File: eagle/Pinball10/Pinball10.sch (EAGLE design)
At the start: 49 parts, among them J1 UB-M5BR-DM14, Q1 MOSFET-NCHANNEL2N7002PW, U1 CYBLE-014008-00, U2 MMA8452Q, U3 PCA9306, U4 V_REG_317SMD

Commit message: labeling done
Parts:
- GND: value PTR1PAD1-13 -> GND
- renumbered JP1 to M0+, JP2 to M1+, LEDBANK0 to BANK0, TP1 to V50, TP2 to GND, TP3 to V33
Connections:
- removed net VDD: LCD.2
- net V50: now also LCD.2
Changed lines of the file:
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@@
 <part name="U$1" library="arh" deviceset="9X2" device=""/>
 <part name="J1" library="con-usb" deviceset="UB-M5BR-DM14" device=""/>
-<part name="LEDBANK0" library="SparkFun-Connectors" deviceset="M08X2" device=""/>
+<part name="BANK0" library="SparkFun-Connectors" deviceset="M08X2" device="" value="M08X2"/>
 <part name="R1" library="SparkFun" deviceset="RESISTOR" device=""/>
 <part name="R2" library="SparkFun" deviceset="RESISTOR" device=""/>
@@
 <part name="R11" library="SparkFun-Resistors" deviceset="RESISTOR" device="0805-RES"/>
 <part name="S1" library="SparkFun-Electromechanical" deviceset="TAC_SWITCH" device="SMD" value="TAC_SWITCHSMD"/>
-<part name="JP1" library="SparkFun-Connectors" deviceset="M02" device="PTH"/>
-<part name="JP2" library="SparkFun-Connectors" deviceset="M02" device="PTH"/>
+<part name="M0+" library="SparkFun-Connectors" deviceset="M02" device="PTH"/>
+<part name="M1+" library="SparkFun-Connectors" deviceset="M02" device="PTH"/>
 <part name="JP3" library="SparkFun-Connectors" deviceset="M05" device="LOCK"/>
 <part name="R12" library="SparkFun-Passives" deviceset="RESISTOR" device="0805-RES"/>
 <part name="R13" library="SparkFun-Passives" deviceset="RESISTOR" device="0805-RES"/>
-<part name="TP1" library="testpad" deviceset="PTR1" device="PAD1-13"/>
-<part name="TP2" library="testpad" deviceset="PTR1" device="PAD1-13"/>
-<part name="TP3" library="testpad" deviceset="PTR1" device="PAD1-13"/>
+<part name="V50" library="testpad" deviceset="PTR1" device="PAD1-13"/>
+<part name="GND" library="testpad" deviceset="PTR1" device="PAD1-13" value="GND"/>
+<part name="V33" library="testpad" deviceset="PTR1" device="PAD1-13"/>
 </parts>
 <sheets>
@@
 </segment>
 </net>
-<net name="VDD" class="0">
-<segment>
-<pinref part="LCD" gate="G$1" pin="2"/>
-<wire x1="86.36" y1="0" x2="101.6" y2="0" width="0.1524" layer="91"/>
-<label x="88.9" y="0" size="1.778" layer="95"/>
-</segment>
-</net>
 <net name="LEDCOL2" class="0">
 <segment>
@@
 <wire x1="116.84" y1="76.2" x2="124.46" y2="76.2" width="0.1524" layer="91"/>
 <label x="116.84" y="76.2" size="1.778" layer="95"/>
+</segment>
+<segment>
+<pinref part="LCD" gate="G$1" pin="2"/>
+<wire x1="86.36" y1="0" x2="101.6" y2="0" width="0.1524" layer="91"/>
+<label x="88.9" y="0" size="1.778" layer="95"/>
 </segment>
 </net>
@@
 </plain>
 <instances>
-<instance part="LEDBANK0" gate="G$1" x="58.42" y="73.66"/>
+<instance part="BANK0" gate="G$1" x="58.42" y="73.66"/>
 <instance part="R1" gate="G$1" x="60.96" y="33.02" rot="R180"/>
 <instance part="R2" gate="G$1" x="60.96" y="20.32" rot="R180"/>
@@
 <net name="LEDROW3" class="0">
 <segment>
-<pinref part="LEDBANK0" gate="G$1" pin="9"/>
+<pinref part="BANK0" gate="G$1" pin="9"/>
 <wire x1="50.8" y1="73.66" x2="33.02" y2="73.66" width="0.1524" layer="91"/>
 <label x="35.56" y="73.66" size="1.778" layer="95"/>
 </segment>
 <segment>
-<pinref part="LEDBANK0" gate="G$1" pin="11"/>
+<pinref part="BANK0" gate="G$1" pin="11"/>
 <wire x1="50.8" y1="71.12" x2="33.02" y2="71.12" width="0.1524" layer="91"/>
 <label x="35.56" y="71.12" size="1.778" layer="95"/>
 </segment>
 <segment>
-<pinref part="LEDBANK0" gate="G$1" pin="13"/>
+<pinref part="BANK0" gate="G$1" pin="13"/>
 <wire x1="50.8" y1="68.58" x2="33.02" y2="68.58" width="0.1524" layer="91"/>
 <label x="35.56" y="68.58" size="1.778" layer="95"/>
 </segment>
 <segment>
-<pinref part="LEDBANK0" gate="G$1" pin="15"/>
+<pinref part="BANK0" gate="G$1" pin="15"/>
 <wire x1="50.8" y1="66.04" x2="33.02" y2="66.04" width="0.1524" layer="91"/>
 <label x="35.56" y="66.04" size="1.778" layer="95"/>
@@
 <net name="LEDROW2" class="0">
 <segment>
-<pinref part="LEDBANK0" gate="G$1" pin="1"/>
+<pinref part="BANK0" gate="G$1" pin="1"/>
 <wire x1="50.8" y1="83.82" x2="33.02" y2="83.82" width="0.1524" layer="91"/>
 <label x="35.56" y="83.82" size="1.778" layer="95"/>
 </segment>
 <segment>
-<pinref part="LEDBANK0" gate="G$1" pin="3"/>
+<pinref part="BANK0" gate="G$1" pin="3"/>
 <wire x1="50.8" y1="81.28" x2="33.02" y2="81.28" width="0.1524" layer="91"/>
 <label x="35.56" y="81.28" size="1.778" layer="95"/>
 </segment>
 <segment>
-<pinref part="LEDBANK0" gate="G$1" pin="5"/>
+<pinref part="BANK0" gate="G$1" pin="5"/>
 <wire x1="50.8" y1="78.74" x2="33.02" y2="78.74" width="0.1524" layer="91"/>
 <label x="35.56" y="78.74" size="1.778" layer="95"/>
 </segment>
 <segment>
-<pinref part="LEDBANK0" gate="G$1" pin="7"/>
+<pinref part="BANK0" gate="G$1" pin="7"/>
 <wire x1="50.8" y1="76.2" x2="33.02" y2="76.2" width="0.1524" layer="91"/>
 <label x="35.56" y="76.2" size="1.778" layer="95"/>
@@
 </segment>
 <segment>
-<pinref part="LEDBANK0" gate="G$1" pin="2"/>
+<pinref part="BANK0" gate="G$1" pin="2"/>
 <wire x1="66.04" y1="83.82" x2="76.2" y2="83.82" width="0.1524" layer="91"/>
 <label x="68.58" y="83.82" size="1.778" layer="95"/>
 </segment>
 <segment>
-<pinref part="LEDBANK0" gate="G$1" pin="10"/>
+<pinref part="BANK0" gate="G$1" pin="10"/>
 <wire x1="66.04" y1="73.66" x2="76.2" y2="73.66" width="0.1524" layer="91"/>
 <label x="68.58" y="73.66" size="1.778" layer="95"/>
@@
 </segment>
 <segment>
-<pinref part="LEDBANK0" gate="G$1" pin="4"/>
+<pinref part="BANK0" gate="G$1" pin="4"/>
 <wire x1="66.04" y1="81.28" x2="76.2" y2="81.28" width="0.1524" layer="91"/>
 <label x="68.58" y="81.28" size="1.778" layer="95"/>
 </segment>
 <segment>
-<pinref part="LEDBANK0" gate="G$1" pin="12"/>
+<pinref part="BANK0" gate="G$1" pin="12"/>
 <wire x1="66.04" y1="71.12" x2="76.2" y2="71.12" width="0.1524" layer="91"/>
 <label x="68.58" y="71.12" size="1.778" layer="95"/>
@@
 </segment>
 <segment>
-<pinref part="LEDBANK0" gate="G$1" pin="6"/>
+<pinref part="BANK0" gate="G$1" pin="6"/>
 <wire x1="66.04" y1="78.74" x2="76.2" y2="78.74" width="0.1524" layer="91"/>
 <label x="68.58" y="78.74" size="1.778" layer="95"/>
 </segment>
 <segment>
-<pinref part="LEDBANK0" gate="G$1" pin="14"/>
+<pinref part="BANK0" gate="G$1" pin="14"/>
 <wire x1="66.04" y1="68.58" x2="76.2" y2="68.58" width="0.1524" layer="91"/>
 <label x="68.58" y="68.58" size="1.778" layer="95"/>
@@
 </segment>
 <segment>
-<pinref part="LEDBANK0" gate="G$1" pin="8"/>
+<pinref part="BANK0" gate="G$1" pin="8"/>
 <wire x1="66.04" y1="76.2" x2="76.2" y2="76.2" width="0.1524" layer="91"/>
 <label x="68.58" y="76.2" size="1.778" layer="95"/>
 </segment>
 <segment>
-<pinref part="LEDBANK0" gate="G$1" pin="16"/>
+<pinref part="BANK0" gate="G$1" pin="16"/>
 <wire x1="66.04" y1="66.04" x2="76.2" y2="66.04" width="0.1524" layer="91"/>
 <label x="68.58" y="66.04" size="1.778" layer="95"/>
@@
 <instances>
 <instance part="HBRIDGE" gate="G$1" x="76.2" y="50.8"/>
-<instance part="JP1" gate="G$1" x="45.72" y="81.28"/>
-<instance part="JP2" gate="G$1" x="93.98" y="81.28"/>
+<instance part="M0+" gate="G$1" x="45.72" y="81.28"/>
+<instance part="M1+" gate="G$1" x="93.98" y="81.28"/>
 </instances>
 <busses>
@@
 <wire x1="53.34" y1="83.82" x2="66.04" y2="83.82" width="0.1524" layer="91"/>
 <label x="55.88" y="83.82" size="1.778" layer="95"/>
-<pinref part="JP1" gate="G$1" pin="2"/>
+<pinref part="M0+" gate="G$1" pin="2"/>
 </segment>
 </net>
@@
 <wire x1="53.34" y1="81.28" x2="66.04" y2="81.28" width="0.1524" layer="91"/>
 <label x="55.88" y="81.28" size="1.778" layer="95"/>
-<pinref part="JP1" gate="G$1" pin="1"/>
+<pinref part="M0+" gate="G$1" pin="1"/>
 </segment>
 </net>
@@
 <wire x1="101.6" y1="83.82" x2="111.76" y2="83.82" width="0.1524" layer="91"/>
 <label x="104.14" y="83.82" size="1.778" layer="95"/>
-<pinref part="JP2" gate="G$1" pin="2"/>
+<pinref part="M1+" gate="G$1" pin="2"/>
 </segment>
 </net>
@@
 <wire x1="101.6" y1="81.28" x2="111.76" y2="81.28" width="0.1524" layer="91"/>
 <label x="104.14" y="81.28" size="1.778" layer="95"/>
-<pinref part="JP2" gate="G$1" pin="1"/>
+<pinref part="M1+" gate="G$1" pin="1"/>
 </segment>
 </net>
@@
 </plain>
 <instances>
-<instance part="TP1" gate="G$1" x="63.5" y="119.38" rot="R270"/>
-<instance part="TP2" gate="G$1" x="63.5" y="111.76" rot="R270"/>
-<instance part="TP3" gate="G$1" x="63.5" y="104.14" rot="R270"/>
+<instance part="V50" gate="G$1" x="63.5" y="119.38" rot="R270"/>
+<instance part="GND" gate="G$1" x="63.5" y="111.76" rot="R270"/>
+<instance part="V33" gate="G$1" x="63.5" y="104.14" rot="R270"/>
 </instances>
 <busses>
@@
 <wire x1="66.04" y1="119.38" x2="73.66" y2="119.38" width="0.1524" layer="91"/>
 <label x="66.04" y="119.38" size="1.778" layer="95"/>
-<pinref part="TP1" gate="G$1" pin="TP"/>
+<pinref part="V50" gate="G$1" pin="TP"/>
 </segment>
 </net>
@@
 <wire x1="66.04" y1="111.76" x2="73.66" y2="111.76" width="0.1524" layer="91"/>
 <label x="66.04" y="111.76" size="1.778" layer="95"/>
-<pinref part="TP2" gate="G$1" pin="TP"/>
+<pinref part="GND" gate="G$1" pin="TP"/>
 </segment>
 </net>
@@
 <wire x1="66.04" y1="104.14" x2="73.66" y2="104.14" width="0.1524" layer="91"/>
 <label x="66.04" y="104.14" size="1.778" layer="95"/>
-<pinref part="TP3" gate="G$1" pin="TP"/>
-</segment>
-</net>
+<pinref part="V33" gate="G$1" pin="TP"/>
+</segment>
+</net>

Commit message: maybe 1.0 board?
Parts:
- M0+, M1+: value M02PTH -> m
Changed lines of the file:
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@@
 <part name="R11" library="SparkFun-Resistors" deviceset="RESISTOR" device="0805-RES"/>
 <part name="S1" library="SparkFun-Electromechanical" deviceset="TAC_SWITCH" device="SMD" value="TAC_SWITCHSMD"/>
-<part name="M0+" library="SparkFun-Connectors" deviceset="M02" device="PTH"/>
-<part name="M1+" library="SparkFun-Connectors" deviceset="M02" device="PTH"/>
+<part name="M0+" library="SparkFun-Connectors" deviceset="M02" device="PTH" value="m"/>
+<part name="M1+" library="SparkFun-Connectors" deviceset="M02" device="PTH" value="m"/>
 <part name="JP3" library="SparkFun-Connectors" deviceset="M05" device="LOCK"/>
 <part name="R12" library="SparkFun-Passives" deviceset="RESISTOR" device="0805-RES"/>

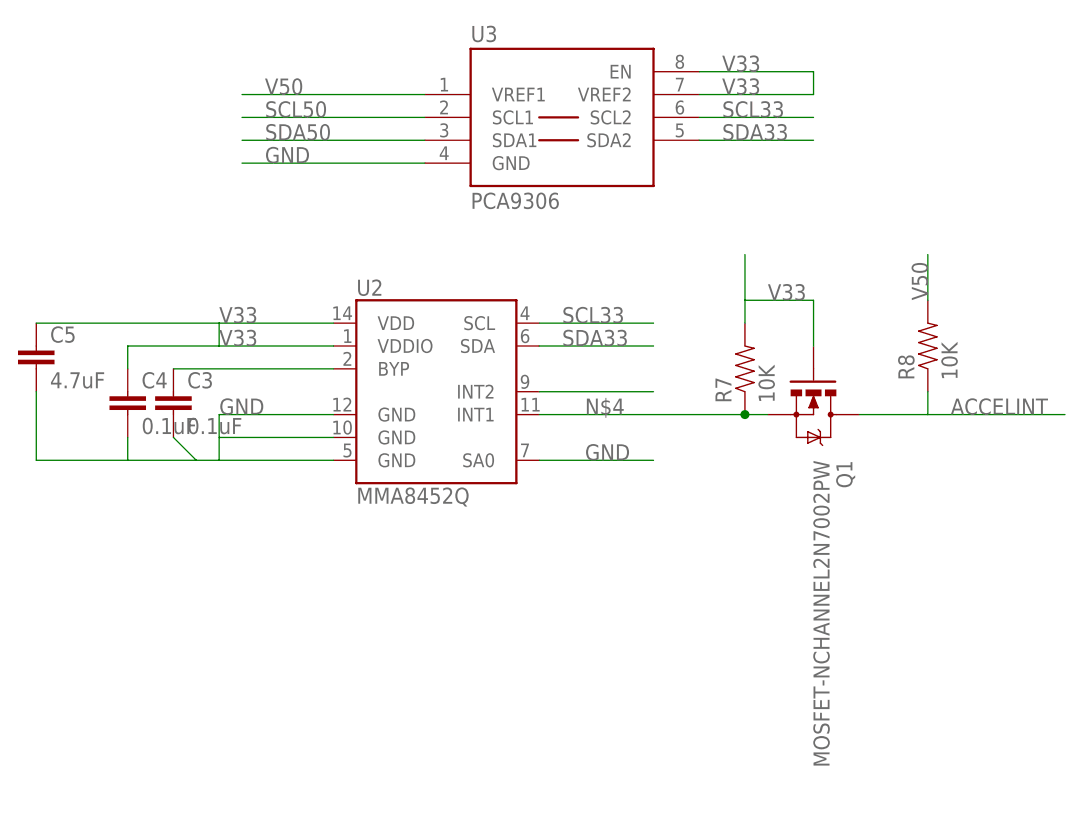
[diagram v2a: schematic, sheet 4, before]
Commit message: fixed errors from ERC (and found a real layout error
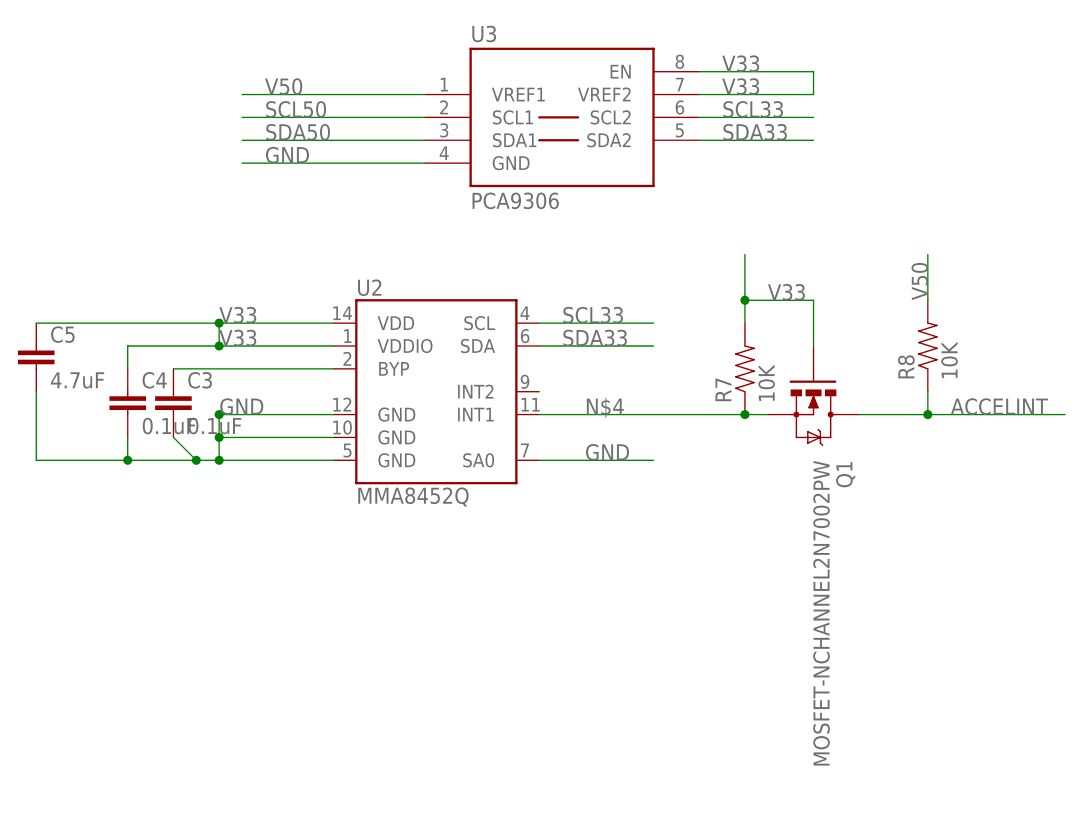
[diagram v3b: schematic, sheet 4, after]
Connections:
- removed net N$29: U2.GND@1
- removed net N$9: U2.INT2
- net GND: now also U2.GND@1
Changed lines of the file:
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@@
 <wire x1="144.78" y1="5.08" x2="144.78" y2="7.62" width="0.1524" layer="91"/>
 <label x="142.24" y="7.62" size="1.778" layer="95"/>
+<junction x="144.78" y="7.62"/>
 </segment>
 </net>
@@
 <wire x1="40.64" y1="96.52" x2="53.34" y2="96.52" width="0.1524" layer="91"/>
 <label x="45.72" y="96.52" size="1.778" layer="95"/>
+<junction x="53.34" y="81.28"/>
 </segment>
 </net>
@@
 <wire x1="71.12" y1="96.52" x2="86.36" y2="96.52" width="0.1524" layer="91"/>
 <label x="76.2" y="96.52" size="1.778" layer="95"/>
+<junction x="86.36" y="81.28"/>
 </segment>
 </net>
@@
 <wire x1="116.84" y1="81.28" x2="116.84" y2="96.52" width="0.1524" layer="91"/>
 <label x="109.22" y="96.52" size="1.778" layer="95"/>
+<junction x="116.84" y="81.28"/>
 </segment>
 </net>
@@
 <wire x1="53.34" y1="68.58" x2="40.64" y2="68.58" width="0.1524" layer="91"/>
 <label x="40.64" y="68.58" size="1.778" layer="95"/>
-<wire x1="40.64" y1="63.5" x2="40.64" y2="68.58" width="0.1524" layer="91"/>
 <pinref part="C5" gate="G$1" pin="2"/>
+<wire x1="40.64" y1="63.5" x2="40.64" y2="66.04" width="0.1524" layer="91"/>
+<wire x1="40.64" y1="66.04" x2="40.64" y2="68.58" width="0.1524" layer="91"/>
 <wire x1="20.32" y1="71.12" x2="20.32" y2="63.5" width="0.1524" layer="91"/>
 <wire x1="20.32" y1="63.5" x2="30.48" y2="63.5" width="0.1524" layer="91"/>
@@
 <pinref part="C4" gate="G$1" pin="2"/>
 <wire x1="30.48" y1="66.04" x2="30.48" y2="63.5" width="0.1524" layer="91"/>
+<junction x="40.64" y="68.58"/>
+<junction x="30.48" y="63.5"/>
+<junction x="38.1" y="63.5"/>
+<junction x="40.64" y="63.5"/>
+<pinref part="U2" gate="G$1" pin="GND@1"/>
+<wire x1="53.34" y1="66.04" x2="40.64" y2="66.04" width="0.1524" layer="91"/>
+<junction x="40.64" y="66.04"/>
 </segment>
 <segment>
@@
 <wire x1="99.06" y1="68.58" x2="101.6" y2="68.58" width="0.1524" layer="91"/>
 <junction x="99.06" y="68.58"/>
-</segment>
-</net>
-<net name="N$9" class="0">
-<segment>
-<pinref part="U2" gate="G$1" pin="INT2"/>
-<wire x1="76.2" y1="71.12" x2="88.9" y2="71.12" width="0.1524" layer="91"/>
 </segment>
 </net>
@@
 <wire x1="40.64" y1="76.2" x2="30.48" y2="76.2" width="0.1524" layer="91"/>
 <wire x1="30.48" y1="76.2" x2="30.48" y2="73.66" width="0.1524" layer="91"/>
+<junction x="40.64" y="76.2"/>
+<junction x="40.64" y="78.74"/>
 </segment>
 <segment>
@@
 <wire x1="106.68" y1="81.28" x2="99.06" y2="81.28" width="0.1524" layer="91"/>
 <label x="101.6" y="81.28" size="1.778" layer="95"/>
+<junction x="99.06" y="81.28"/>
 </segment>
 </net>
@@
 <wire x1="53.34" y1="73.66" x2="35.56" y2="73.66" width="0.1524" layer="91"/>
 <pinref part="C3" gate="G$1" pin="1"/>
-</segment>
-</net>
-<net name="N$29" class="0">
-<segment>
-<pinref part="U2" gate="G$1" pin="GND@1"/>
-<wire x1="53.34" y1="66.04" x2="40.64" y2="66.04" width="0.1524" layer="91"/>
 </segment>
 </net>
@@
 <wire x1="119.38" y1="71.12" x2="119.38" y2="68.58" width="0.1524" layer="91"/>
 <label x="121.92" y="68.58" size="1.778" layer="95"/>
+<junction x="119.38" y="68.58"/>
 </segment>
 </net>
@@
 <wire x1="45.72" y1="78.74" x2="58.42" y2="78.74" width="0.1524" layer="91"/>
 <wire x1="45.72" y1="76.2" x2="45.72" y2="78.74" width="0.1524" layer="91"/>
+<junction x="45.72" y="78.74"/>
 </segment>
 </net>
@@
 <wire x1="45.72" y1="48.26" x2="45.72" y2="43.18" width="0.1524" layer="91"/>
 <label x="17.78" y="43.18" size="1.778" layer="95"/>
+<junction x="45.72" y="43.18"/>
 </segment>
 </net>
@@
 <wire x1="45.72" y1="60.96" x2="22.86" y2="60.96" width="0.1524" layer="91"/>
 <wire x1="22.86" y1="60.96" x2="22.86" y2="71.12" width="0.1524" layer="91"/>
-</segment>
-</net>
+<junction x="45.72" y="60.96"/>
+</segment>
+</net>

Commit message: final 1.0c board
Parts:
- renumbered SG2 to 1
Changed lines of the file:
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@@
 <part name="D9" library="SparkFun-DiscreteSemi" deviceset="DIODE" device="SOD"/>
 <part name="SG1" library="SparkFun-Electromechanical" deviceset="BUZZER" device="PTH"/>
-<part name="SG2" library="SparkFun-Electromechanical" deviceset="BUZZER" device="PTH"/>
+<part name="1" library="SparkFun-Electromechanical" deviceset="BUZZER" device="PTH"/>
 <part name="B0" library="PatternAgents-TouchWidgets" deviceset="BUTTON_PASSIVE" device="12MM"/>
 <part name="LCD" library="SparkFun-Connectors" deviceset="M04" device="JST-PTH"/>
@@
 <instance part="J1" gate="G$1" x="48.26" y="99.06"/>
 <instance part="SG1" gate="G$1" x="88.9" y="88.9" rot="R90"/>
-<instance part="SG2" gate="G$1" x="129.54" y="88.9" rot="R90"/>
+<instance part="1" gate="G$1" x="129.54" y="88.9" rot="R90"/>
 <instance part="B0" gate="B1" x="129.54" y="30.48" rot="R180"/>
 <instance part="LCD" gate="G$1" x="81.28" y="0"/>
@@
 </segment>
 <segment>
-<pinref part="SG2" gate="G$1" pin="2"/>
+<pinref part="1" gate="G$1" pin="2"/>
 <wire x1="132.08" y1="91.44" x2="142.24" y2="91.44" width="0.1524" layer="91"/>
 <label x="134.62" y="91.44" size="1.778" layer="95"/>
@@
 </segment>
 <segment>
-<pinref part="SG2" gate="G$1" pin="1"/>
+<pinref part="1" gate="G$1" pin="1"/>
 <wire x1="132.08" y1="88.9" x2="142.24" y2="88.9" width="0.1524" layer="91"/>
 <label x="134.62" y="88.9" size="1.778" layer="95"/>
